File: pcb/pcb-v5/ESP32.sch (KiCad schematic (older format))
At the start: 4 parts, among them U1 AMS1117-3.3

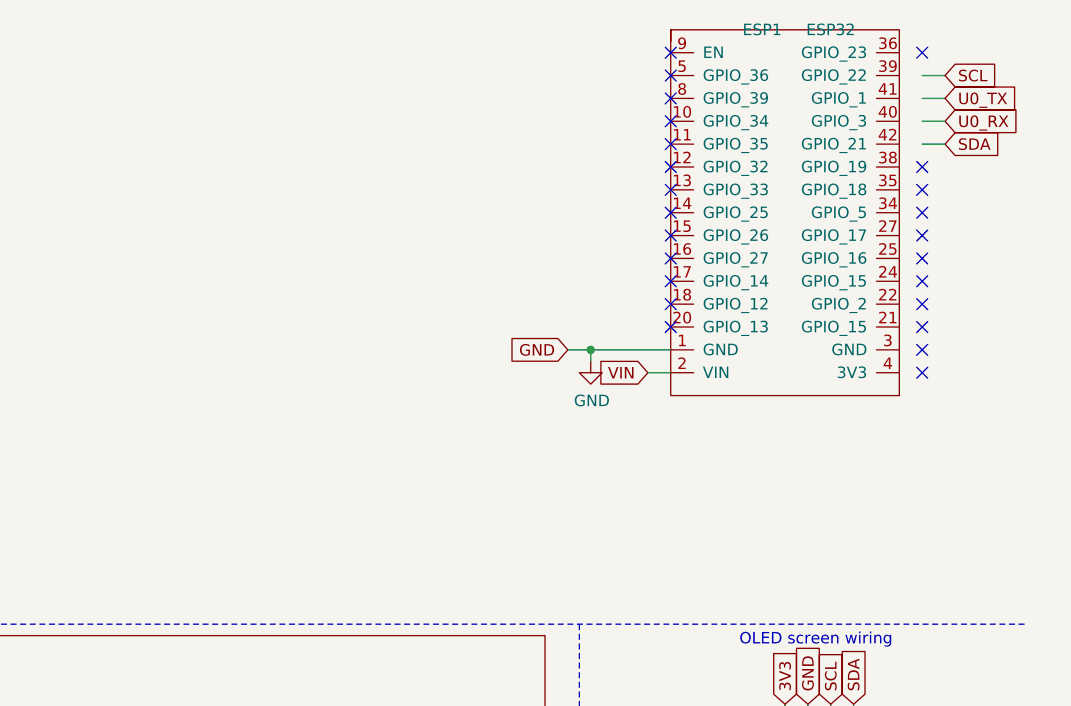
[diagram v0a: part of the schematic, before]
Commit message: PCB-V5 updated
Added 2 mounting holes and 2x4pins connectors
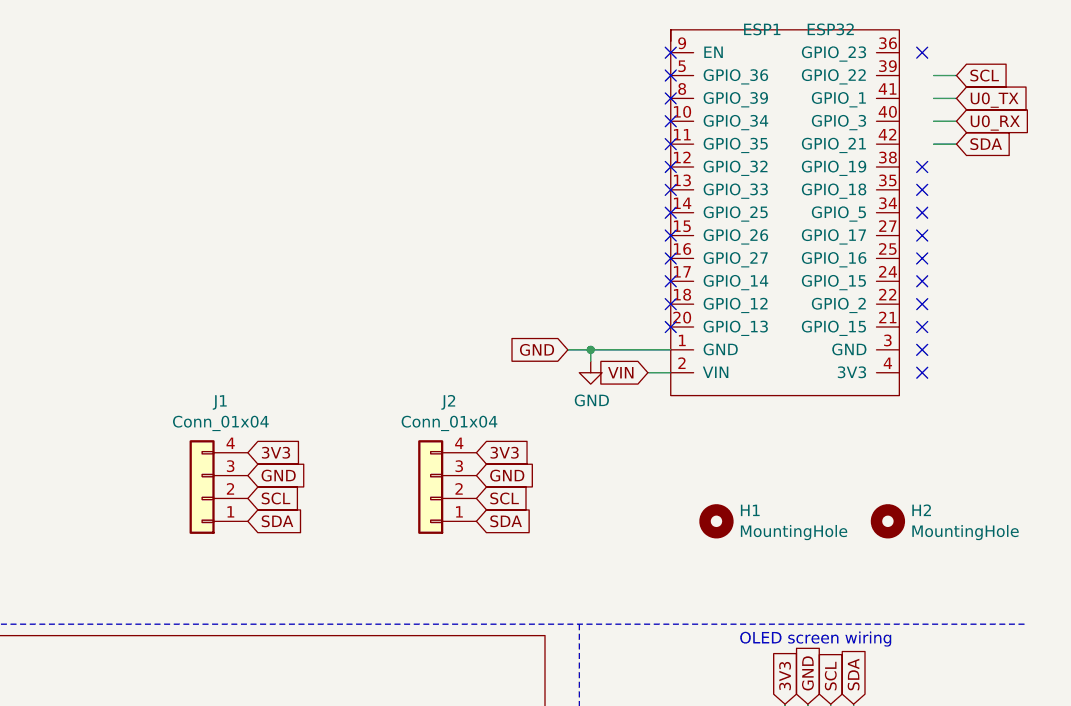
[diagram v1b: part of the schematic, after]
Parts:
- added H1, H2: MountingHole, MountingHole:MountingHole_2.5mm, symbol Mechanical:MountingHole
- added J1, J2: Conn_01x04, Connector_PinHeader_2.54mm:PinHeader_1x04_P2.54mm_Vertical, symbol Connector_Generic:Conn_01x04
- ESP1: footprint (none) -> pcb-v5:ESP32_30_pins
- OLED1: footprint (none) -> pcb-v5:OLED_1.3
- SDS111: footprint (none) -> pcb-v5:SDS011
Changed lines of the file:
@@
 Wire Notes Line
 	9250 6500 11200 6500
-Text GLabel 10850 900  2    50   Input ~ 0
-SCL
-Text GLabel 10850 1200 2    50   Input ~ 0
-SDA
-Wire Wire Line
-	10750 900  10850 900
-Wire Wire Line
-	10750 1200 10850 1200
+Text GLabel 10900 900  2    50   Input ~ 0
+SCL
+Text GLabel 10900 1200 2    50   Input ~ 0
+SDA
+Wire Wire Line
+	10800 900  10900 900
+Wire Wire Line
+	10800 1200 10900 1200
 Text GLabel 10150 3650 1    50   Input ~ 0
 3V3
@@
 Wire Notes Line
 	9250 3300 9250 6500
-Text GLabel 10850 1000 2    50   Input ~ 0
+Text GLabel 10900 1000 2    50   Input ~ 0
 U0_TX
-Text GLabel 10850 1100 2    50   Input ~ 0
+Text GLabel 10900 1100 2    50   Input ~ 0
 U0_RX
 Wire Wire Line
-	10750 1000 10850 1000
-Wire Wire Line
-	10750 1100 10850 1100
+	10800 1000 10900 1000
+Wire Wire Line
+	10800 1100 10900 1100
 $Comp
 L sensOCampus:ESP32 ESP1
@@
 F 0 "ESP1" H 10050 3700 50  0000 C CNN
 F 1 "ESP32" H 10350 3700 50  0000 C CNN
-F 2 "" H 9650 2200 50  0001 C CNN
+F 2 "pcb-v5:ESP32_30_pins" H 9650 2200 50  0001 C CNN
 F 3 "" H 9650 2200 50  0001 C CNN
 	1    9650 2200
@@
 F 0 "OLED1" H 10550 5000 50  0000 L CNN
 F 1 "OLED_1.3\"" H 9800 5000 50  0000 L CNN
-F 2 "" H 9600 5050 50  0001 C CNN
+F 2 "pcb-v5:OLED_1.3" H 9600 5050 50  0001 C CNN
 F 3 "" H 9600 5050 50  0001 C CNN
 	1    9600 5050
@@
 F 0 "SDS111" H 7350 6050 50  0000 L CNN
 F 1 "SDS011" H 6750 6050 50  0000 L CNN
-F 2 "" H 6350 6100 50  0001 C CNN
+F 2 "pcb-v5:SDS011" H 6350 6100 50  0001 C CNN
 F 3 "" H 6350 6100 50  0001 C CNN
 	1    6350 6100
@@
 	1    0    0    -1
 $EndComp
+$Comp
+L Mechanical:MountingHole H1
+U 1 1 60086E03
+P 9850 2850
+F 0 "H1" H 9950 2896 50  0000 L CNN
+F 1 "MountingHole" H 9950 2805 50  0000 L CNN
+F 2 "MountingHole:MountingHole_2.5mm" H 9850 2850 50  0001 C CNN
+F 3 "~" H 9850 2850 50  0001 C CNN
+	1    9850 2850
+	1    0    0    -1
+$EndComp
+$Comp
+L Mechanical:MountingHole H2
+U 1 1 60088AAF
+P 10600 2850
+F 0 "H2" H 10700 2896 50  0000 L CNN
+F 1 "MountingHole" H 10700 2805 50  0000 L CNN
+F 2 "MountingHole:MountingHole_2.5mm" H 10600 2850 50  0001 C CNN
+F 3 "~" H 10600 2850 50  0001 C CNN
+	1    10600 2850
+	1    0    0    -1
+$EndComp
+$Comp
+L Connector_Generic:Conn_01x04 J2
+U 1 1 60089A77
+P 8600 2750
+F 0 "J2" H 8518 2325 50  0000 C CNN
+F 1 "Conn_01x04" H 8518 2416 50  0000 C CNN
+F 2 "Connector_PinHeader_2.54mm:PinHeader_1x04_P2.54mm_Vertical" H 8600 2750 50  0001 C CNN
+F 3 "~" H 8600 2750 50  0001 C CNN
+	1    8600 2750
+	-1   0    0    1
+$EndComp
+$Comp
+L Connector_Generic:Conn_01x04 J1
+U 1 1 6008B377
+P 7600 2750
+F 0 "J1" H 7518 2325 50  0000 C CNN
+F 1 "Conn_01x04" H 7518 2416 50  0000 C CNN
+F 2 "Connector_PinHeader_2.54mm:PinHeader_1x04_P2.54mm_Vertical" H 7600 2750 50  0001 C CNN
+F 3 "~" H 7600 2750 50  0001 C CNN
+	1    7600 2750
+	-1   0    0    1
+$EndComp
+Text GLabel 8800 2550 2    50   Input ~ 0
+3V3
+Text GLabel 8800 2650 2    50   Input ~ 0
+GND
+Text GLabel 8800 2750 2    50   Input ~ 0
+SCL
+Text GLabel 8800 2850 2    50   Input ~ 0
+SDA
+Text GLabel 7800 2550 2    50   Input ~ 0
+3V3
+Text GLabel 7800 2650 2    50   Input ~ 0
+GND
+Text GLabel 7800 2750 2    50   Input ~ 0
+SCL
+Text GLabel 7800 2850 2    50   Input ~ 0
+SDA
 $EndSCHEMATC

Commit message: PCB-V5 update
PCB updated for presentation
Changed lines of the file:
@@
 Wire Notes Line
 	9250 6500 11200 6500
-Text GLabel 10900 900  2    50   Input ~ 0
+Text GLabel 10850 900  2    50   Input ~ 0
 SCL
-Text GLabel 10900 1200 2    50   Input ~ 0
+Text GLabel 10850 1200 2    50   Input ~ 0
 SDA
 Wire Wire Line
-	10800 900  10900 900
+	10750 900  10850 900
 Wire Wire Line
-	10800 1200 10900 1200
+	10750 1200 10850 1200
 Text GLabel 10150 3650 1    50   Input ~ 0
 3V3
@@
 Wire Notes Line
 	9250 3300 9250 6500
-Text GLabel 10900 1000 2    50   Input ~ 0
+Text GLabel 10850 1000 2    50   Input ~ 0
 U0_TX
-Text GLabel 10900 1100 2    50   Input ~ 0
+Text GLabel 10850 1100 2    50   Input ~ 0
 U0_RX
 Wire Wire Line
-	10800 1000 10900 1000
+	10750 1000 10850 1000
 Wire Wire Line
-	10800 1100 10900 1100
+	10750 1100 10850 1100
 $Comp
 L sensOCampus:ESP32 ESP1

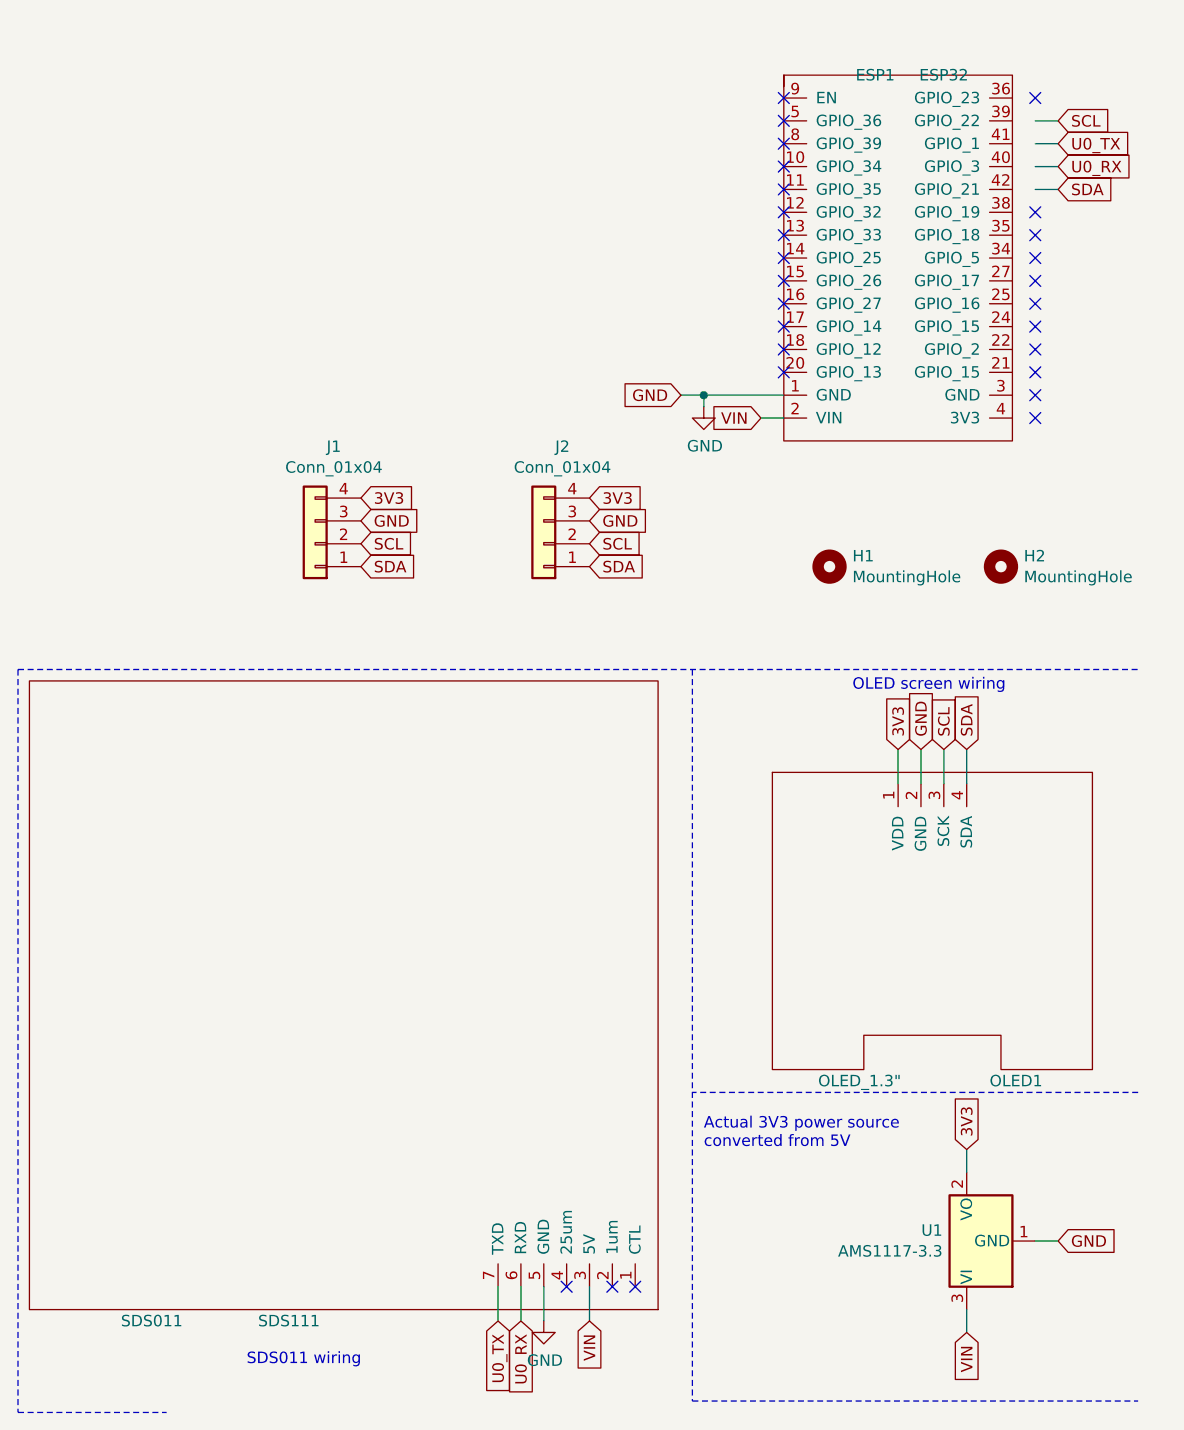
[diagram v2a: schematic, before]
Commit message: ESP32 board update
Added 3 buttons and 1 LED.
Added metallized AMS1117 back
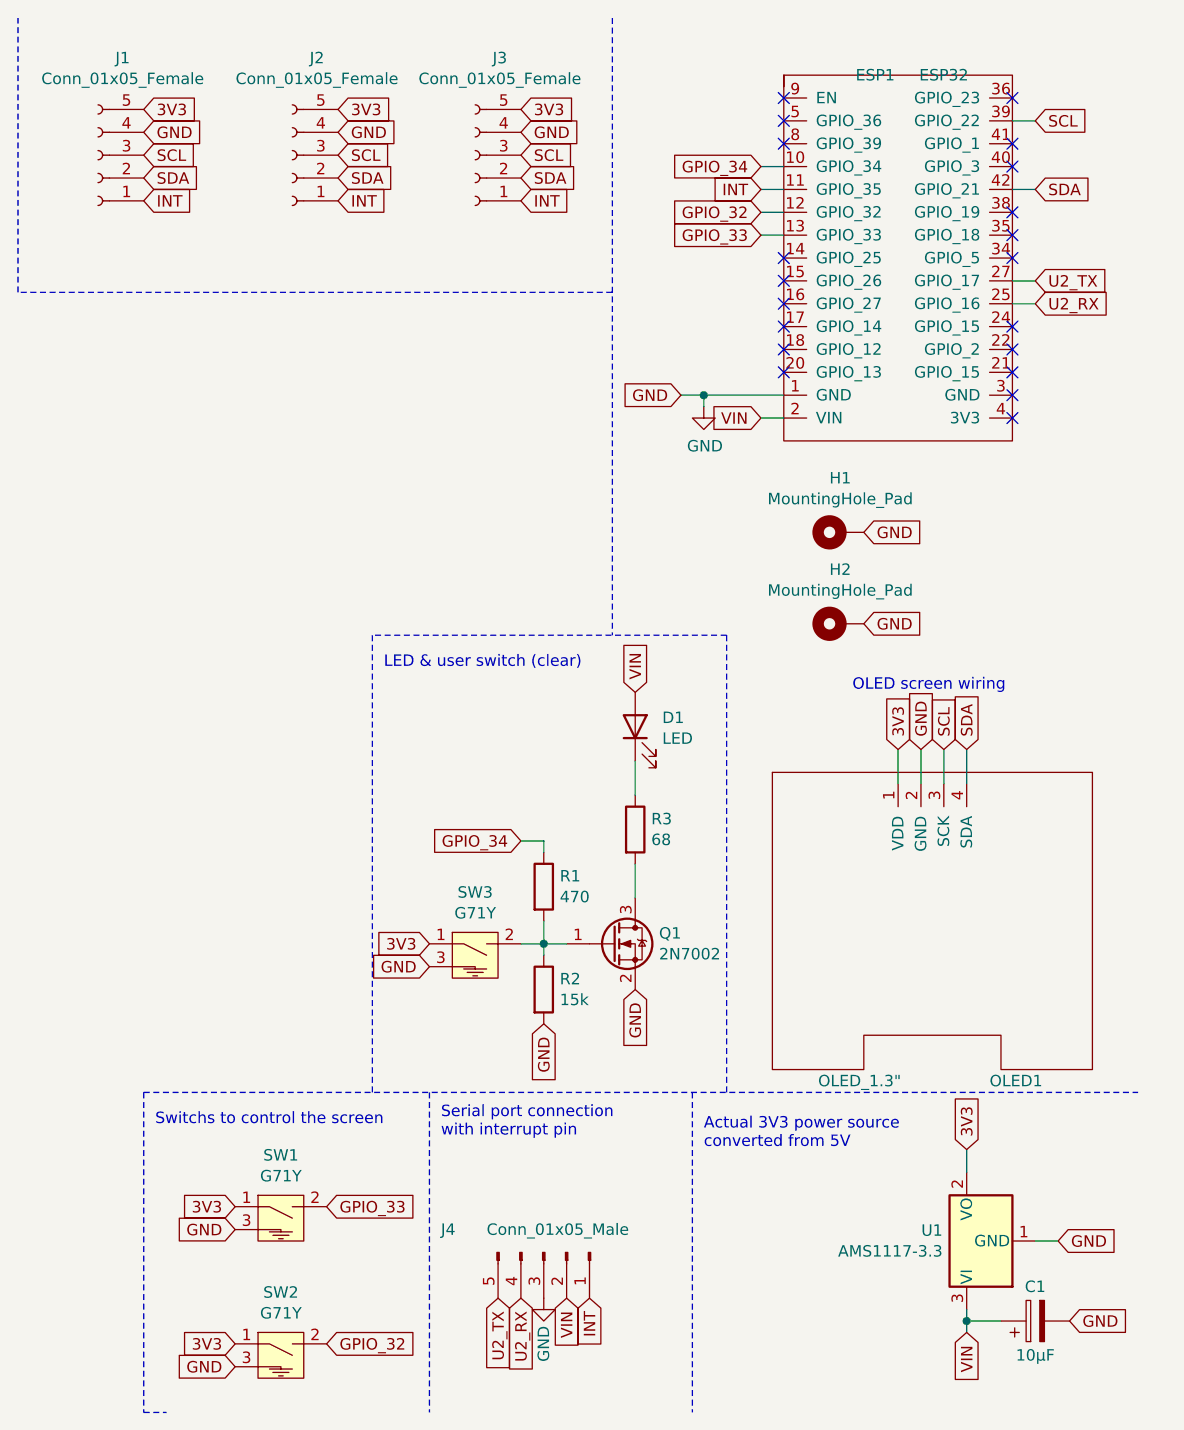
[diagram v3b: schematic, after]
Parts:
- removed H1, H2: MountingHole, MountingHole:MountingHole_2.5mm, symbol Mechanical:MountingHole
- removed J1, J2: Conn_01x04, Connector_PinHeader_2.54mm:PinHeader_1x04_P2.54mm_Vertical, symbol Connector_Generic:Conn_01x04
- removed SDS111: SDS011, pcb-v5:SDS011, symbol sensOCampus:SDS011
- added C1: 10µF, Capacitor_SMD:C_0805_2012Metric_Pad1.18x1.45mm_HandSolder, symbol Device:CP
- added D1: LED, LED_SMD:LED_0805_2012Metric_Pad1.15x1.40mm_HandSolder, symbol Device:LED
- added H1, H2: MountingHole_Pad, MountingHole:MountingHole_3.2mm_M3_Pad, symbol Mechanical:MountingHole_Pad
- added J1, J2, J3: Conn_01x05_Female, Connector_PinHeader_2.54mm:PinHeader_1x05_P2.54mm_Vertical, symbol Connector:Conn_01x05_Female
- added J4: Conn_01x05_Male, Connector_PinHeader_2.54mm:PinHeader_1x05_P2.54mm_Vertical, symbol Connector:Conn_01x05_Male
- added Q1: 2N7002, Package_TO_SOT_SMD:SOT-23, symbol Transistor_FET:2N7002
- added R1: 470, Resistor_SMD:R_0805_2012Metric_Pad1.20x1.40mm_HandSolder, symbol Device:R
- added R2: 15k, Resistor_SMD:R_0805_2012Metric_Pad1.20x1.40mm_HandSolder, symbol Device:R
- added R3: 68, Resistor_SMD:R_0805_2012Metric_Pad1.20x1.40mm_HandSolder, symbol Device:R
- added SW1, SW2, SW3: G71Y, pcb-v5:G71Y_µsw_smd, symbol neosensor_addon:G71Y
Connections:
- net labels added: GPIO_32, GPIO_33, GPIO_34, INT, U2_RX, U2_TX
- net labels removed: U0_RX, U0_TX
- wire segments 19 -> 29
- no-connect marks 27 -> 20
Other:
- note added: "LED & user switch (clear)"
- note added: "Serial port connection\nwith interrupt pin"
- note added: "Switchs to control the screen"
- note removed: "SDS011 wiring"
